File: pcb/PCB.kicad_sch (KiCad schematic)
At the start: 35 parts, among them J1 Conn_01x15, J2 USB_C_Receptacle_USB2.0, J3 Conn_01x15, J4 TC2030, J5 Conn_01x04, SW1 SW_Push, SW2 SW_Push, U1 SN65HVD230, U2 AMS1117-3.3, U3 STM32F103C8T6, Y1 8MHz

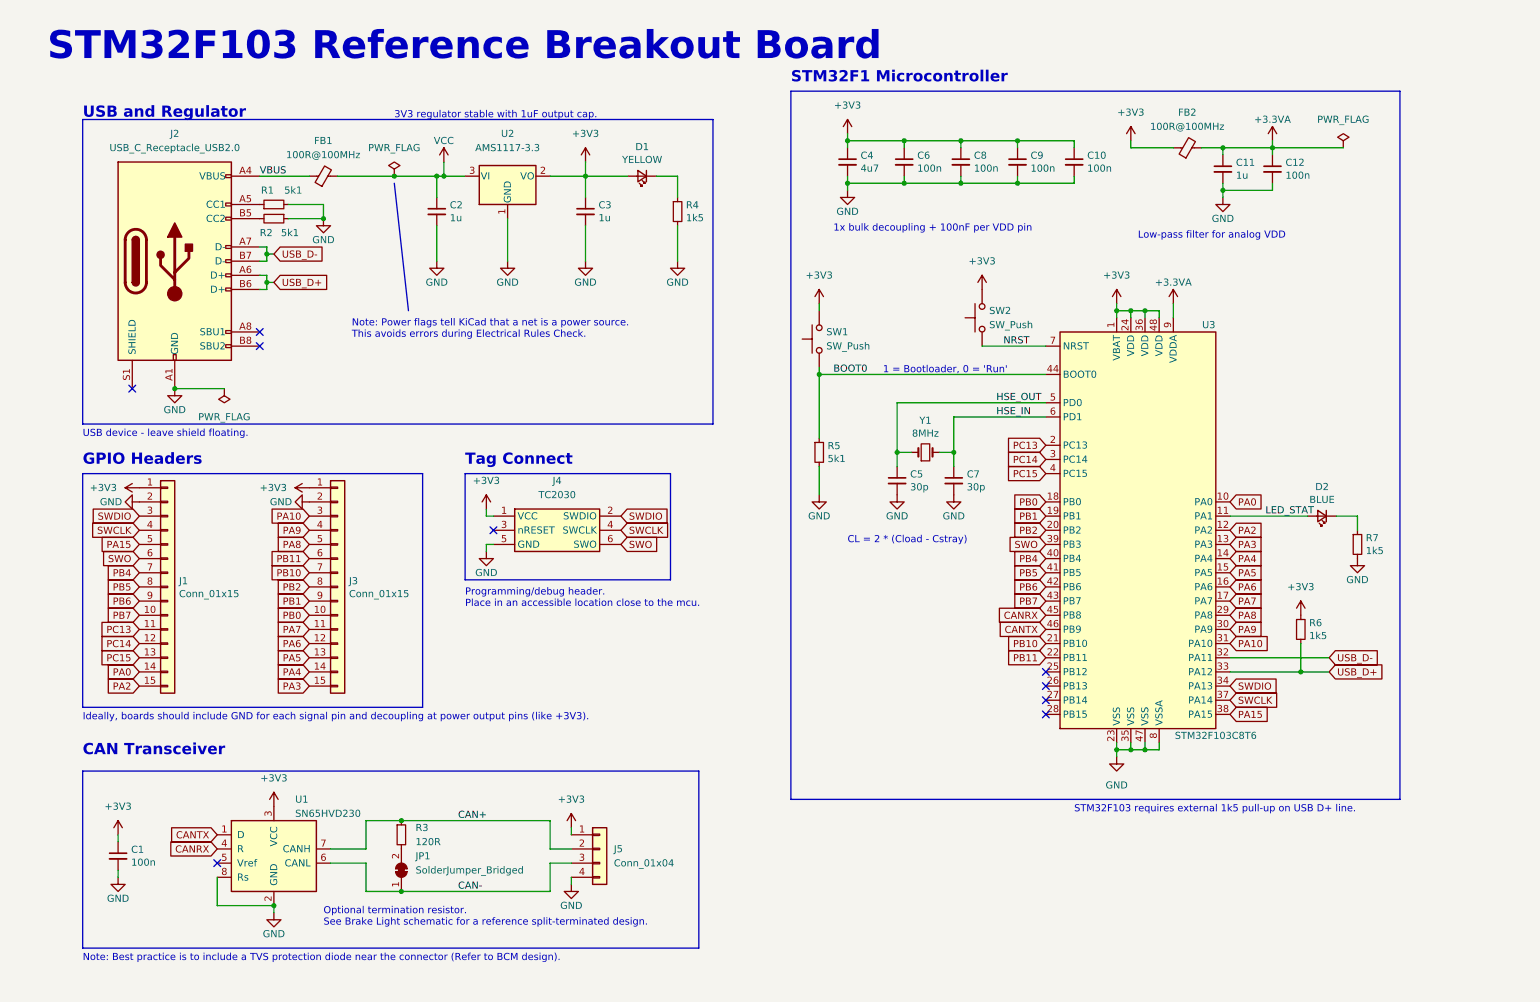
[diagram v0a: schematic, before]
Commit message: created schematic and layout of the telemetry board
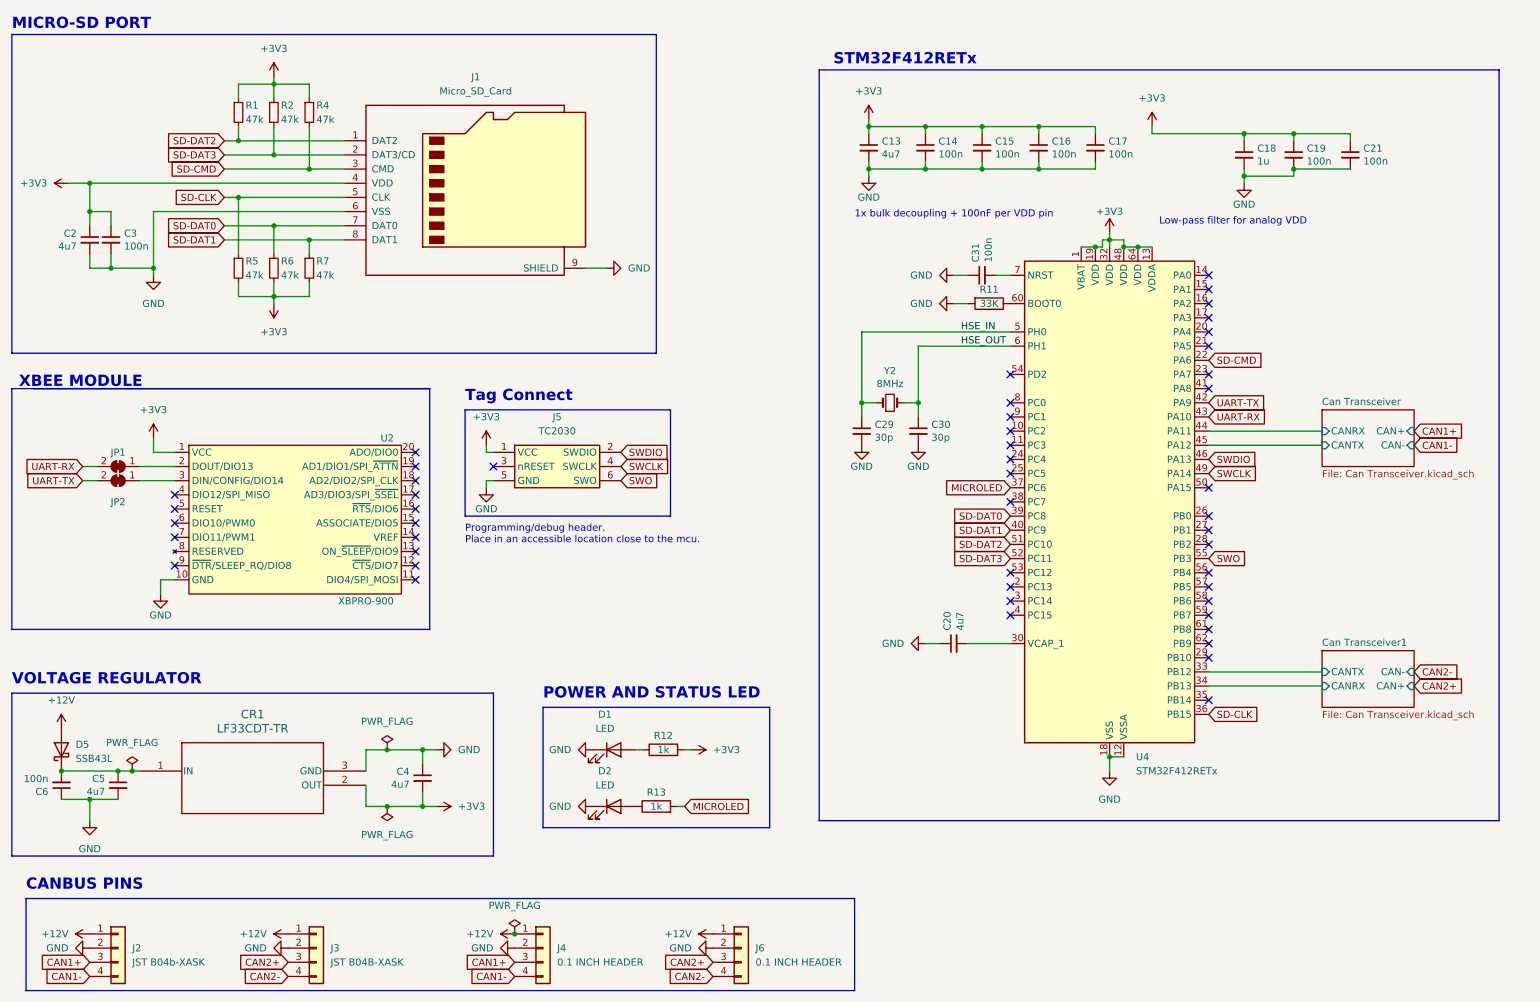
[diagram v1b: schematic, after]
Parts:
- removed C1, C10, C12, C8, C9: 100n, Capacitor_SMD:C_0402_1005Metric, symbol Device:C_Small
- removed C11: 1u, Capacitor_SMD:C_0603_1608Metric, symbol Device:C_Small
- removed C7: 30p, Capacitor_SMD:C_0402_1005Metric, symbol Device:C_Small
- removed D1: YELLOW, LED_SMD:LED_0603_1608Metric, symbol Device:LED_Small
- removed D2: BLUE, LED_SMD:LED_0603_1608Metric, symbol Device:LED_Small
- removed FB1, FB2: 100R@100MHz, Resistor_SMD:R_0805_2012Metric, symbol Device:FerriteBead_Small
- removed J1, J3: Conn_01x15, Connector_PinHeader_2.54mm:PinHeader_1x15_P2.54mm_Vertical, symbol Connector_Generic:Conn_01x15
- removed J2: USB_C_Receptacle_USB2.0, Connector_USB:USB_C_Receptacle_HRO_TYPE-C-31-M-12, symbol Connector:USB_C_Receptacle_USB2.0
- removed J4: TC2030, Connector:Tag-Connect_TC2030-IDC-NL_2x03_P1.27mm_Vertical, symbol TC2030:TC2030
- removed J5: Conn_01x04, Connector_PinHeader_2.54mm:PinHeader_1x04_P2.54mm_Vertical, symbol Connector_Generic:Conn_01x04
- removed R3: 120R, Resistor_SMD:R_0402_1005Metric, symbol Device:R_Small
- removed SW1, SW2: SW_Push, Button_Switch_SMD:SW_Push_1P1T_NO_CK_KSC7xxJ, symbol Switch:SW_Push
- removed U1: SN65HVD230, Package_SO:SOIC-8_3.9x4.9mm_P1.27mm, symbol Interface_CAN_LIN:SN65HVD230
- removed U2: AMS1117-3.3, Package_TO_SOT_SMD:SOT-223-3_TabPin2, symbol Regulator_Linear:AMS1117-3.3
- removed U3: STM32F103C8T6, Package_QFP:LQFP-48_7x7mm_P0.5mm, symbol MCU_ST_STM32F1:STM32F103C8Tx
- removed Y1: 8MHz, Crystal:Crystal_SMD_5032-2Pin_5.0x3.2mm, symbol Device:Crystal_Small
- added C13, C20: 4u7, Capacitor_SMD:C_0603_1608Metric, symbol Device:C_Small
- added C14, C15, C16, C17, C19, C21, C31: 100n, Capacitor_SMD:C_0603_1608Metric, symbol Device:C_Small
- added C18: 1u, Capacitor_SMD:C_0603_1608Metric, symbol Device:C_Small
- added C29, C30: 30p, Capacitor_SMD:C_0603_1608Metric, symbol Device:C_Small
- added CR1: LF33CDT-TR, LF33CDT:DPAK_STM, symbol 2023-10-25_21-36-40:LF33CDT-TR
- added D1, D2: LED, LED_SMD:LED_0603_1608Metric, symbol Device:LED
- added D5: SSB43L, Diode_SMD:D_SMB, symbol Device:D_Schottky
- added J1: Micro_SD_Card, Connector_Card:microSD_HC_Wuerth_693072010801, symbol Connector:Micro_SD_Card
- added J2: JST B04b-XASK, Connector_JST:JST_XA_B04B-XASK-1_1x04_P2.50mm_Vertical, symbol Connector_Generic:Conn_01x04
- added J3: JST B04B-XASK, Connector_JST:JST_XA_B04B-XASK-1-A_1x04_P2.50mm_Vertical, symbol Connector_Generic:Conn_01x04
- added J4, J6: 0.1 INCH HEADER, Connector_PinHeader_2.54mm:PinHeader_1x04_P2.54mm_Vertical, symbol Connector_Generic:Conn_01x04
- added J5: TC2030, Connector:Tag-Connect_TC2030-IDC-NL_2x03_P1.27mm_Vertical, symbol TC2030:TC2030
- added JP2: SolderJumper_2_Bridged, Jumper:SolderJumper-2_P1.3mm_Bridged_RoundedPad1.0x1.5mm, symbol Jumper:SolderJumper_2_Bridged
- added R11: 33K, Resistor_SMD:R_0603_1608Metric, symbol Device:R
- added R12, R13: 1k, Resistor_SMD:R_0603_1608Metric, symbol Device:R
- added U2: XBPRO-900, XBEE:XBEEPRO900HP, symbol XBEE:XBP9B-DSMT-012
- added U4: STM32F412RETx, Package_QFP:LQFP-64_10x10mm_P0.5mm, symbol MCU_ST_STM32F4:STM32F412RETx
- added Y2: 8MHz, Crystal:Crystal_SMD_5032-2Pin_5.0x3.2mm, symbol Device:Crystal_Small
- C2: value 1u -> 4u7; LCSC C15849 -> C19666
- C3: value 1u -> 100n; LCSC C15849 -> C307331
- C5: value 30p -> 4u7; footprint Capacitor_SMD:C_0402_1005Metric -> Capacitor_SMD:C_0603_1608Metric; LCSC C1570 -> C19666
- C6: footprint Capacitor_SMD:C_0402_1005Metric -> Capacitor_SMD:C_0603_1608Metric
- JP1: value SolderJumper_Bridged -> SolderJumper_2_Bridged
- R1, R2, R5: value 5k1 -> 47k; footprint Resistor_SMD:R_0402_1005Metric -> Resistor_SMD:R_0603_1608Metric; LCSC C25905 -> (none)
- R4, R6, R7: value 1k5 -> 47k; footprint Resistor_SMD:R_0402_1005Metric -> Resistor_SMD:R_0603_1608Metric; LCSC C25867 -> (none)
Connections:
- net USB_D+ is gone; now on net +3V3: R6.2
- net VCC is gone; now on net +3V3: C2.1
- net +3V3: now also C4.2, R1.1, R2.1, R4.1, R5.2, R7.2, C13.1, C14.1, C15.1, C16.1, C17.1, C18.1, C19.1, C21.1, CR1.2 (OUT), J1.4 (VDD), J5.1 (VCC), R12.2, U2.1 (VCC), U4.1 (VBAT), U4.13 (VDDA), U4.19 (VDD), U4.32 (VDD), U4.48 (VDD), U4.64 (VDD); no longer C4.1, C6.1, R6.1
- net GND: now also C4.1, C6.1, C13.2, C14.2, C15.2, C16.2, C17.2, C18.2, C19.2, C20.1, C21.2, C29.2, C30.2, C31.1, CR1.3 (GND), D1.1 (K), D2.1 (K), J1.6 (VSS), J1.9 (SHIELD), J2.2 (Pin_2), J3.2 (Pin_2), J4.2 (Pin_2), J5.5 (GND), J6.2 (Pin_2), R11.2, U2.10 (GND), U4.12 (VSSA), U4.18 (VSS), U4.31 (VSS), U4.47 (VSS), U4.63 (VSS); no longer C4.2, C6.2, R1.2, R2.1, R4.2, R5.2, R7.2
- net HSE_IN: now also C29.1, U4.5 (PH0), Y2.1
- net HSE_OUT: now also C30.1, U4.6 (PH1), Y2.2; no longer C5.1
- net SWCLK: now also J5.4 (SWCLK), U4.49 (PA14)
- net SWDIO: now also J5.2 (SWDIO), U4.46 (PA13)
- net SWO: now also J5.6 (SWO), U4.55 (PB3)
- net UART-RX: now reaches JP1.2 (B)
- net UART-RX: now also U4.43 (PA10)
- net SD-DAT1: now reaches R7.1
- net SD-DAT1: now also J1.8 (DAT1), U4.40 (PC9)
- net SD-DAT3: now reaches R2.2
- net SD-DAT3: now also J1.2 (DAT3/CD), U4.52 (PC11)
- net BOOT0 renamed SD-CLK
- net SD-CLK: now also J1.5 (CLK), U4.36 (PB15)
- net CAN-: no longer names the net of JP1.1 (A)
- net CAN-: now also U2.2 (DOUT/DIO13)
- new net: C5.1, C6.2, CR1.1 (IN), D5.1 (K)
- new net: JP2.1 (A), U2.3 (DIN/CONFIG/DIO14)
- new net: C20.2, U4.30 (VCAP_1)
- new net: R11.1, U4.60 (BOOT0)
- new net: D2.2 (A), R13.1
- new net: D1.2 (A), R12.1
- new net: C31.2, U4.7 (NRST)
- new net +12V: D5.2 (A), J2.1 (Pin_1), J3.1 (Pin_1), J4.1 (Pin_1), J6.1 (Pin_1)
- new net CAN1+: J2.3 (Pin_3), J4.3 (Pin_3)
- new net CAN1-: J2.4 (Pin_4), J4.4 (Pin_4)
- new net CAN2+: J3.3 (Pin_3), J6.3 (Pin_3)
- new net CAN2-: J3.4 (Pin_4), J6.4 (Pin_4)
- new net Can Transceiver/CANRX: U4.44 (PA11)
- new net Can Transceiver/CANTX: U4.45 (PA12)
- new net Can Transceiver1/CANRX: U4.34 (PB13)
- new net Can Transceiver1/CANTX: U4.33 (PB12)
- new net MICROLED: R13.2, U4.37 (PC6)
- new net SD-CMD: J1.3 (CMD), R4.2, U4.22 (PA6)
- new net SD-DAT0: J1.7 (DAT0), R6.1, U4.39 (PC8)
- new net SD-DAT2: J1.1 (DAT2), R1.2, U4.51 (PC10)
- new net UART-TX: JP2.2 (B), U4.42 (PA9)
- no-connect marks 9 -> 48
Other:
- added sheet Can Transceiver (Can Transceiver.kicad_sch)
- added sheet Can Transceiver1 (Can Transceiver.kicad_sch)
- note added: "CANBUS PINS"
- note added: "MICRO-SD PORT"
- note added: "POWER AND STATUS LED"
- note added: "STM32F412RETx"
- note added: "VOLTAGE REGULATOR"
- note added: "XBEE MODULE"
- note removed: "1 = Bootloader, 0 = 'Run'"
- note removed: "3V3 regulator stable with 1uF output cap."
- note removed: "CAN Transceiver"
- note removed: "CL = 2 * (Cload - Cstray)"
- note removed: "GPIO Headers"
- note removed: "Ideally, boards should include GND for each signal pin and decoupling at power output pins (like +3V3)."
- note removed: "Note: Best practice is to include a TVS protection diode near the connector (Refer to BCM design)."
- note removed: "Note: Power flags tell KiCad that a net is a power source. This avoids errors during Electrical Rules Check."
- note removed: "Optional termination resistor. See Brake Light schematic for a reference split-terminated design."
- note removed: "STM32F1 Microcontroller"
- note removed: "STM32F103 Reference Breakout Board"
- note removed: "STM32F103 requires external 1k5 pull-up on USB D+ line."
- note removed: "USB and Regulator"
- note removed: "USB device - leave shield floating."
